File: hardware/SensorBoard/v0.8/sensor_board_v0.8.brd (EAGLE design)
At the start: 52.5 x 43 mm, 48 parts, among them IC1 BMP280, J3 USB-MICROB, U1 ATMEGA328P, U10 CCS811, U11 RFM69HW, U2 TSL2561, U5 FT231XS, U7 SHT31, U8 MCP1703/3.3V, U9 MCP1703CB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

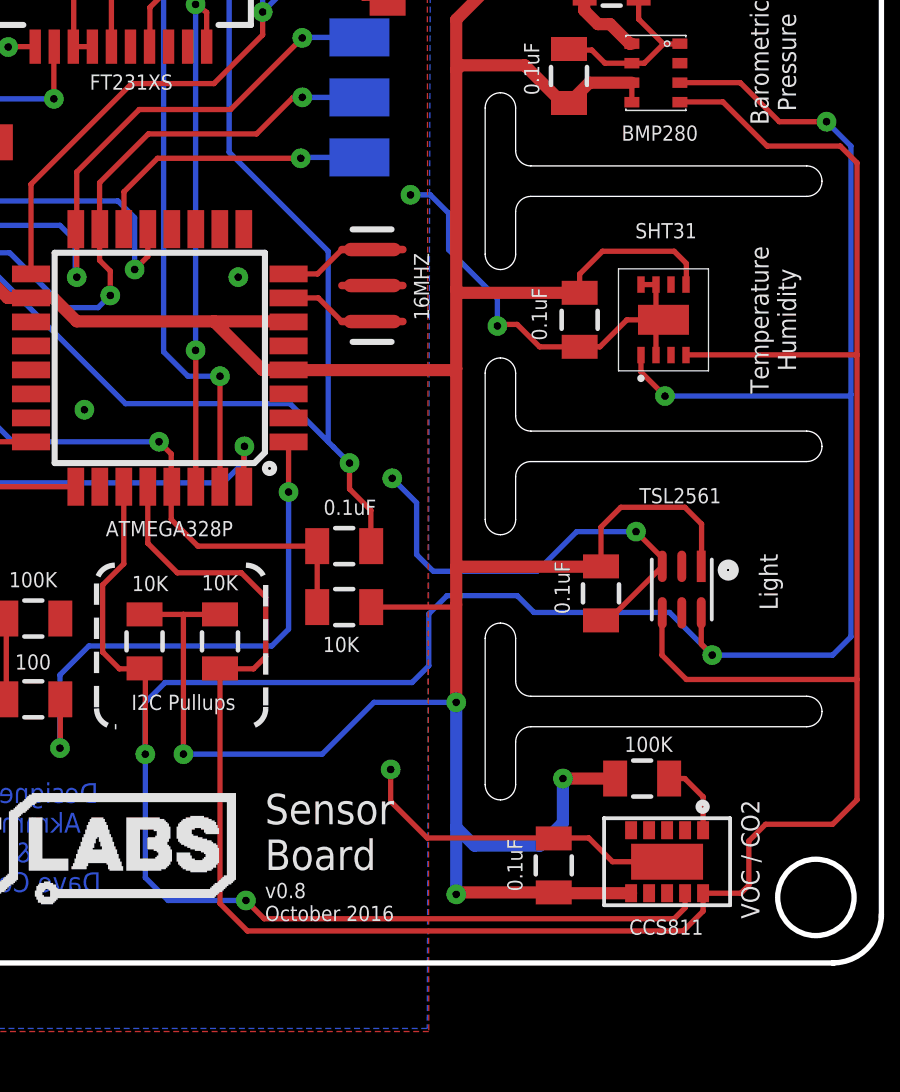
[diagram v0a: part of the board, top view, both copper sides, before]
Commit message: Added traces for WAKE and INT pin
CCS811 requires WAKE pin to be triggered before every communication. INT
can be useful in the future for lower power or threshold alerts.
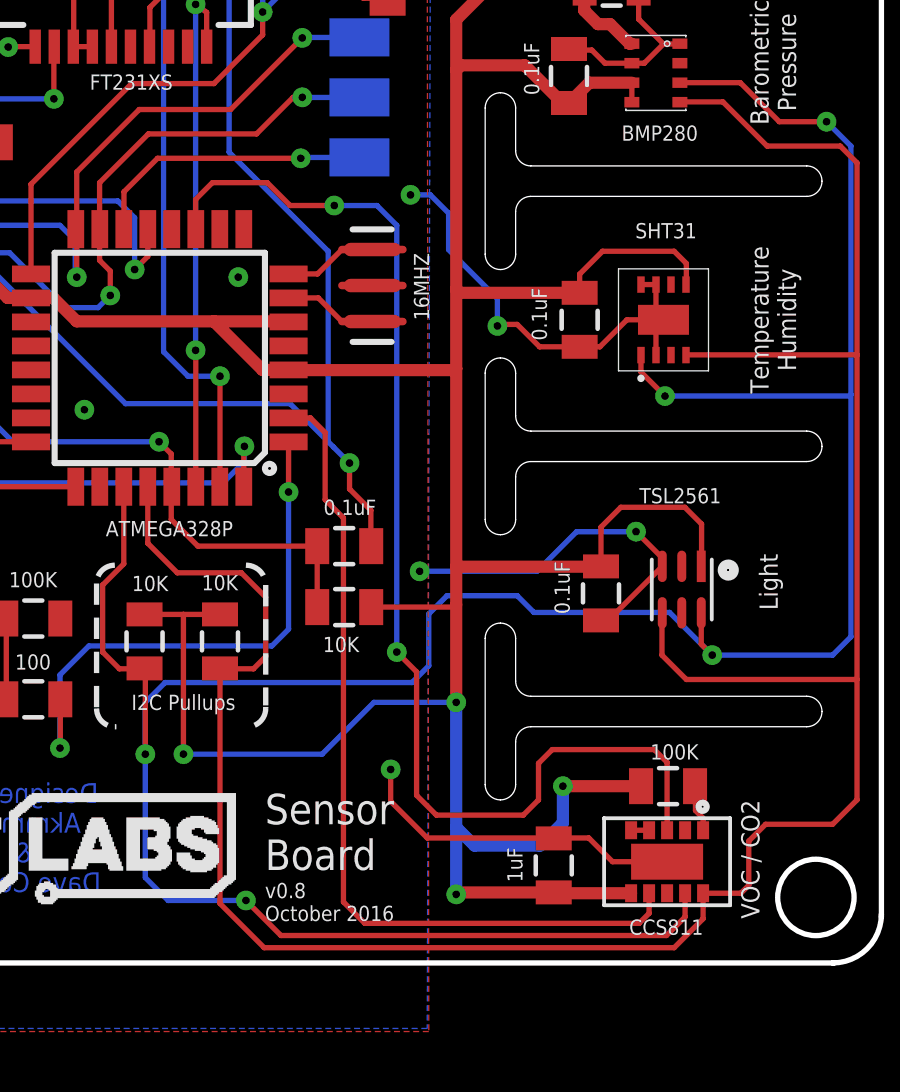
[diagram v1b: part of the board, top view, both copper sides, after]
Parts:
- C5: value 0.1uF -> 1uF
- moved R2 0.90 mm to (48.8, 11.8)
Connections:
- new net INT: U1.11, U10.3
- new net N$6: U10.4, U10.5
- new net WAKE: U1.2, U10.7
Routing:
- net INT: track 0.00 -> 40.5 mm, vias 0 -> 2
- net WAKE: track 0.00 -> 28.6 mm
- net GND: track 60.0 -> 56.8 mm
- net N$1: track 2.50 -> 1.82 mm
- net SDA: track 94.8 -> 95.5 mm
- net SCL: track 84.7 -> 85.3 mm
- net VCC: track 146.0 -> 146.7 mm
- net N$6: track 0.00 -> 0.60 mm

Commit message: Replaced ATmega328P TQFP with QFN/MLF Package
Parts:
- removed U1: ATMEGA328P, SparkFun-DigitalIC:TQFP32-08
- added U3: ATMEGA328P-MU, ATMEGA328P-MU:QFN50P500X500X100-33N
- moved Y1 3.93 mm to (35.1, 28.9)
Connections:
- net A0: now also U3.23; no longer U1.23
- net A7: now also U3.22; no longer U1.22
- net D2: now also U3.32; no longer U1.32
- net D5: now also U3.9; no longer U1.9
- net GND: now also U3.21, U3.3, U3.33, U3.5; no longer U1.21, U1.3, U1.5
- net INT: now also U3.11; no longer U1.11
- net MISO: now also U3.16; no longer U1.16
- net MOSI: now also U3.15; no longer U1.15
- net N$2: now also U3.13; no longer U1.13
- net N$4: now also U3.8; no longer U1.8
- net N$5: now also U3.7; no longer U1.7
- net PRE: now also U3.1; no longer U1.1
- net RESET: now also U3.29; no longer U1.29
- net RX: now also U3.30; no longer U1.30
- net SCK: now also U3.17; no longer U1.17
- net SCL: now also U3.28; no longer U1.28
- net SDA: now also U3.27; no longer U1.27
- net SS: now also U3.14; no longer U1.14
- net TX: now also U3.31; no longer U1.31
- net VCC: now also U3.18, U3.4, U3.6; no longer U1.18, U1.4, U1.6
- net VNOX: now also U3.24; no longer U1.24
- net VRED: now also U3.25; no longer U1.25
- net WAKE: now also U3.2; no longer U1.2
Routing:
- net VCC: track 146.7 -> 158.6 mm, vias 5 -> 8
- net GND: track 56.8 -> 66.5 mm, vias 33 -> 34
- net D2: track 29.8 -> 35.5 mm
- net PRE: track 18.6 -> 22.8 mm
- net WAKE: track 28.6 -> 32.7 mm
- net DTR: track 57.1 -> 60.9 mm, vias 2 -> 3
- net SCL: track 85.3 -> 88.2 mm
- net INT: track 40.5 -> 43.0 mm
- net RX: track 58.0 -> 60.4 mm
- net SDA: track 95.5 -> 97.7 mm
- net SS: track 9.57 -> 11.8 mm
- net MOSI: track 45.0 -> 43.1 mm
- net RESET: track 51.1 -> 52.8 mm
- net TX: track 52.0 -> 50.4 mm
- net VNOX: track 30.9 -> 32.4 mm
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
